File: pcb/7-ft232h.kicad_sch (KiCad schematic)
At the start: 0 parts

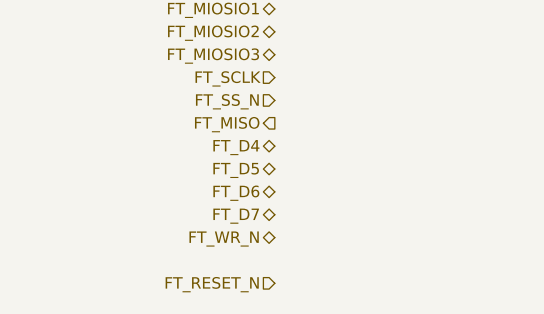
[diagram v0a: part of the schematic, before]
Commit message: Phase 3: populate power sheet; descriptive net names
Power sheet: bench eFuse (TPS259470A) with UVLO/OVLO string and EN
clamp, TPS2116 bench-priority mux with VBUS snubber, 3.3 V and 2.83 V
TPS73701 LDOs. Notes on the string's tap voltages, eFuse setting pins
and every DNP part. Project symbol library with the TPS259470A and
TPS73701DCQ drawn from the datasheet pin tables.

Nets renamed to spelled-out names (IS_BENCH_POWERED, *_INVERTED for
active-low, FEEDBACK, VTERMINATOR, TERMINATOR_EN) across the schematic,
pinout page, parts list and power block page.

Co-Authored-By: Claude Opus 5.5 <noreply@anthropic.com>
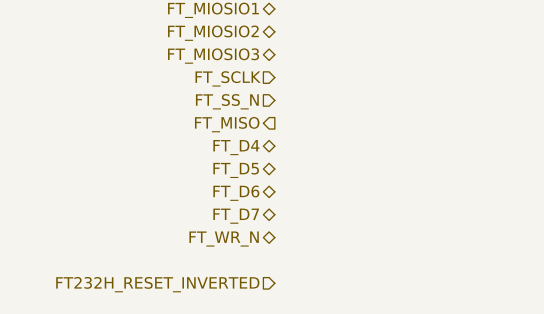
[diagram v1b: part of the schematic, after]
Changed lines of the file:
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@@
 	(hierarchical_label "FT_D7" (shape bidirectional) (at 50.8 76.2 180) (effects (font (size 1.27 1.27)) (justify right)))
 	(hierarchical_label "FT_WR_N" (shape bidirectional) (at 50.8 78.74 180) (effects (font (size 1.27 1.27)) (justify right)))
-	(hierarchical_label "FT_RESET_N" (shape input) (at 50.8 83.82 180) (effects (font (size 1.27 1.27)) (justify right)))
+	(hierarchical_label "FT232H_RESET_INVERTED" (shape input) (at 50.8 83.82 180) (effects (font (size 1.27 1.27)) (justify right)))
 	(hierarchical_label "USB_FT_D+" (shape bidirectional) (at 343.8 50.8 0) (effects (font (size 1.27 1.27)) (justify left)))
 	(hierarchical_label "USB_FT_D-" (shape bidirectional) (at 343.8 53.34 0) (effects (font (size 1.27 1.27)) (justify left)))
